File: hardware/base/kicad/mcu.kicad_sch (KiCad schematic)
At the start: 33 parts, among them J5 TC2030, SW1 BOOT, U9 STM32H523VET6

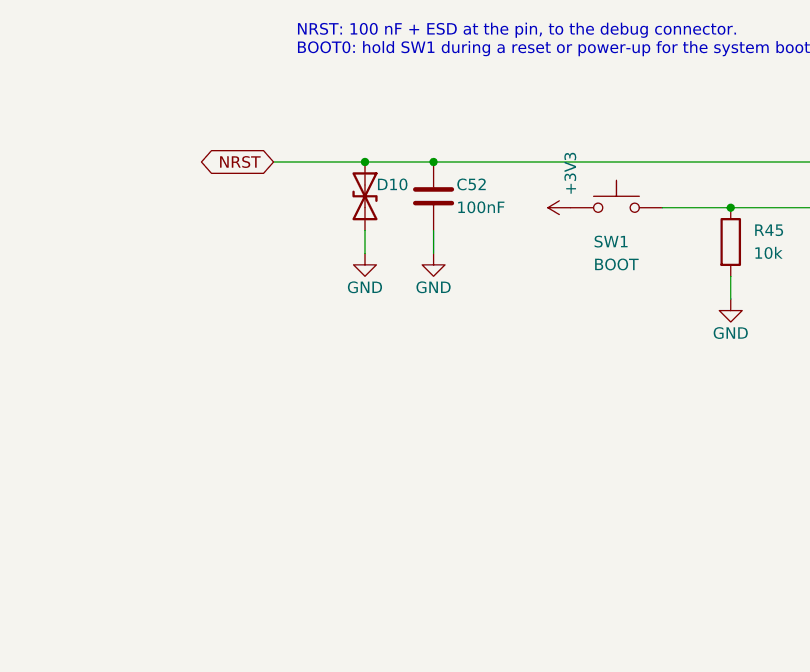
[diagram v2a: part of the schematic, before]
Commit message: Trim the base board BOM: 60 to 58 lines
- ESD of NRST and of the PWM output on one channel of the TPD4E05U06
  already used on the PHY lines, instead of a PESD5V0S1BA.
- SS56B instead of SS34 for the 5 V / USB OR-ing and the encoder
  supplies.
- One 100 uF 10 V X5R 1210 on the 5 V buck output instead of two 47 uF:
  about 55 uF at 5 V, inside the simulated 34-80 uF.
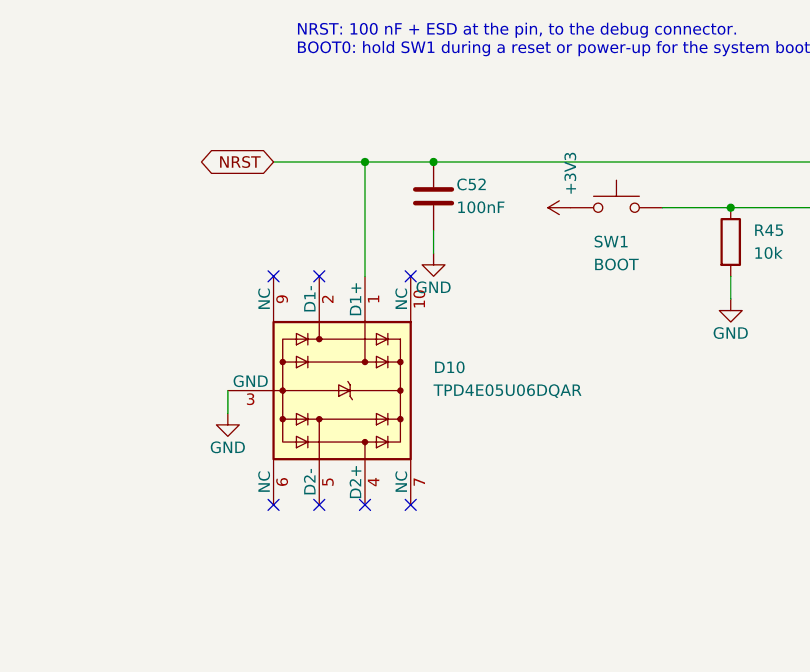
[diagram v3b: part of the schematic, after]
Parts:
- D10: value PESD5V0S1BA -> TPD4E05U06DQAR; footprint Diode_SMD:D_SOD-323 -> Package_SON:USON-10_2.5x1.0mm_P0.5mm; symbol Device:D_TVS -> Power_Protection:TPD4E05U06DQA; LCSC C19224 -> C138714
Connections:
- net GND: now also D10.3 (GND), D10.8 (GND); no longer D10.2 (A2)
- no-connect marks 0 -> 7

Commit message: Differential pairs routed by script; PHY to jack mapping for a planar layout
- pairs.py, pass "pairs" right after the planes and trunks: A* on a 0.1 mm
  grid for the centre line of each pair, clear of the other copper by about
  3 W (by the clearance alone near the pads), offset into its two lines;
  straight out of the QFN pads, straight through the ESD arrays, each line on
  its own into the through-hole pins of the jack. Ethernet 100 ohm and USB
  90 ohm at 0.15 mm gap (sim/impedance.py).
- Schematic: the lines on the jack pins and ESD channels in the order that
  routes without a crossing (port A with P and N swapped, port B with TX and
  RX swapped: the LAN9253 PHYs correct the polarity and have HP Auto-MDIX);
  the NC pins of the ESD arrays opposite each line carry it (TI flow-through).
- Ethernet terminations lifted off the board while the pairs are routed, then
  put against their line, 2 to 10 mm from the PHY pins; the lines inside a
  port straddled by their 0603 termination (49.9 ohm moved to 0603, C23185,
  basic, 1.78 M in stock on 2026-10-20; clock series resistors too).
- Placement: lanes of the pairs kept free of other parts (LAN9253 checklist);
  ESD arrays in the way of their lines; centre tap capacitors at the jacks;
  VDD33TXRX mini-planes in layer 3 under the terminations.
- route.py: real C-LOCK cutout clearance for copper; via hole to pad
  clearance; mini-plane priority in the plane test.
- kicadgen: tagged labels do not name a net (a second label on a NC pin).

Claude-Session: https://claude.ai/code/session_01D6Na26JP4CWdxCU6BKa4Yc
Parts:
- R47, R48, R49, R50, R51, R52: footprint Resistor_SMD:R_0402_1005Metric -> Resistor_SMD:R_0603_1608Metric; LCSC C25120 -> C23185

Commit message: USB jack, its ESD and VBUS sense on the MCU sheet; channel and block checks; renet and unroute of the working board
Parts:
- added J2: USB micro-B, Connector_USB:USB_Micro-B_Molex-105133-0001, symbol Connector:USB_B_Micro
- added R7: 1k, Resistor_SMD:R_0402_1005Metric, symbol Device:R
- added R8: 2.2k, Resistor_SMD:R_0402_1005Metric, symbol Device:R
- added U2: TPD4E05U06DQAR, Package_SON:USON-10_2.5x1.0mm_P0.5mm, symbol Power_Protection:TPD4E05U06DQA
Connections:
- net GND: now also J2.5 (GND), J2.SH (Shield), R8.2, U2.3 (GND), U2.8 (GND)
- net USB_DM: now also J2.2 (D-), U2.2 (D1-), U2.9 (NC)
- net USB_DP: now also J2.3 (D+), U2.1 (D1+), U2.10 (NC)
- net VBUS_SENSE: now also R7.2, R8.1
- new net VBUS: J2.1 (VBUS), R7.1, U2.5 (D2-), U2.6 (NC)
- no-connect marks 7 -> 10
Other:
- note added: "USB micro-B: bench power (logic only) and DFU programming. TPD4E05U06 next to the connector, lines flow through."
- note added: "VBUS_SENSE on PD9: 3.4 V, 5 V tolerant pin; an input (USART3_RX) in the bootloader."
- title: MCU STM32H523VET6, decoupling, debug -> MCU STM32H523VET6, decoupling, debug, USB
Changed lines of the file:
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@@
 	(paper "A3")
 	(title_block
-		(title "MCU STM32H523VET6, decoupling, debug")
+		(title "MCU STM32H523VET6, decoupling, debug, USB")
 		(date "2026-10-18")
 		(rev "A")
